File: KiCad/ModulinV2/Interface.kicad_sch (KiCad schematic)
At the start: 37 parts, among them IC2 ADS7866IDBVT, IC3 ADS7866IDBVT, IC4 ADS7041IDCUR, IC5 ADS7041IDCUR, IC6 DAC60501ZDGSR, IC7 DAC60501ZDGSR

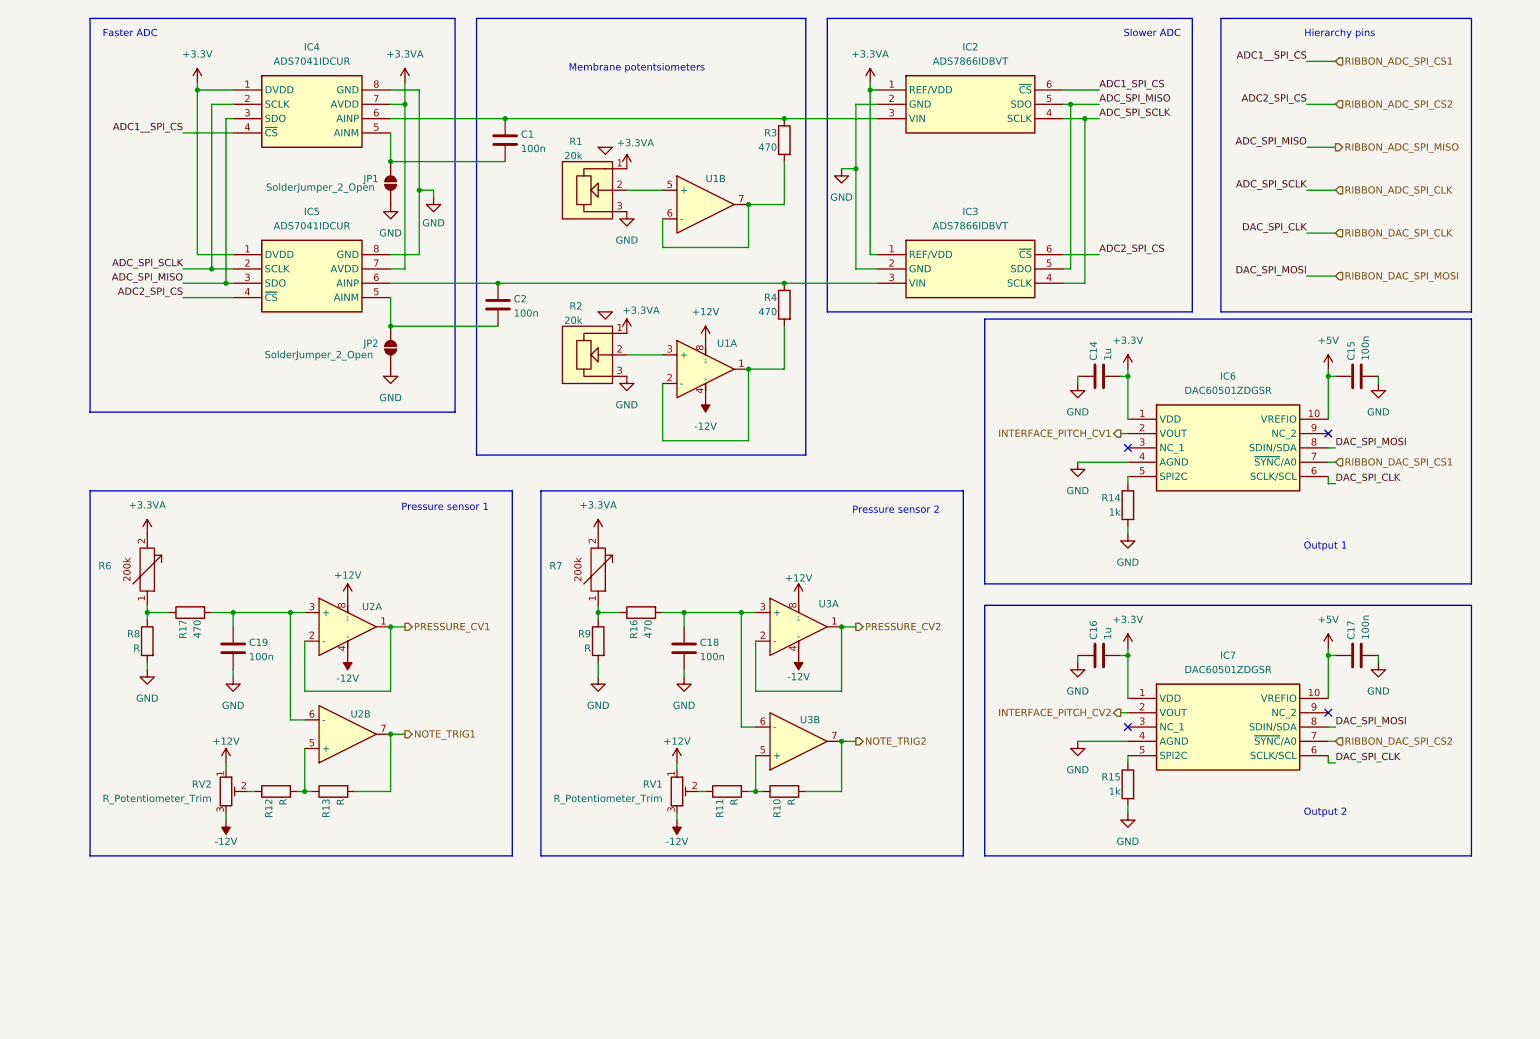
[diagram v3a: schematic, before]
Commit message: Added initial schematic of VCO and repaired some schematic issues
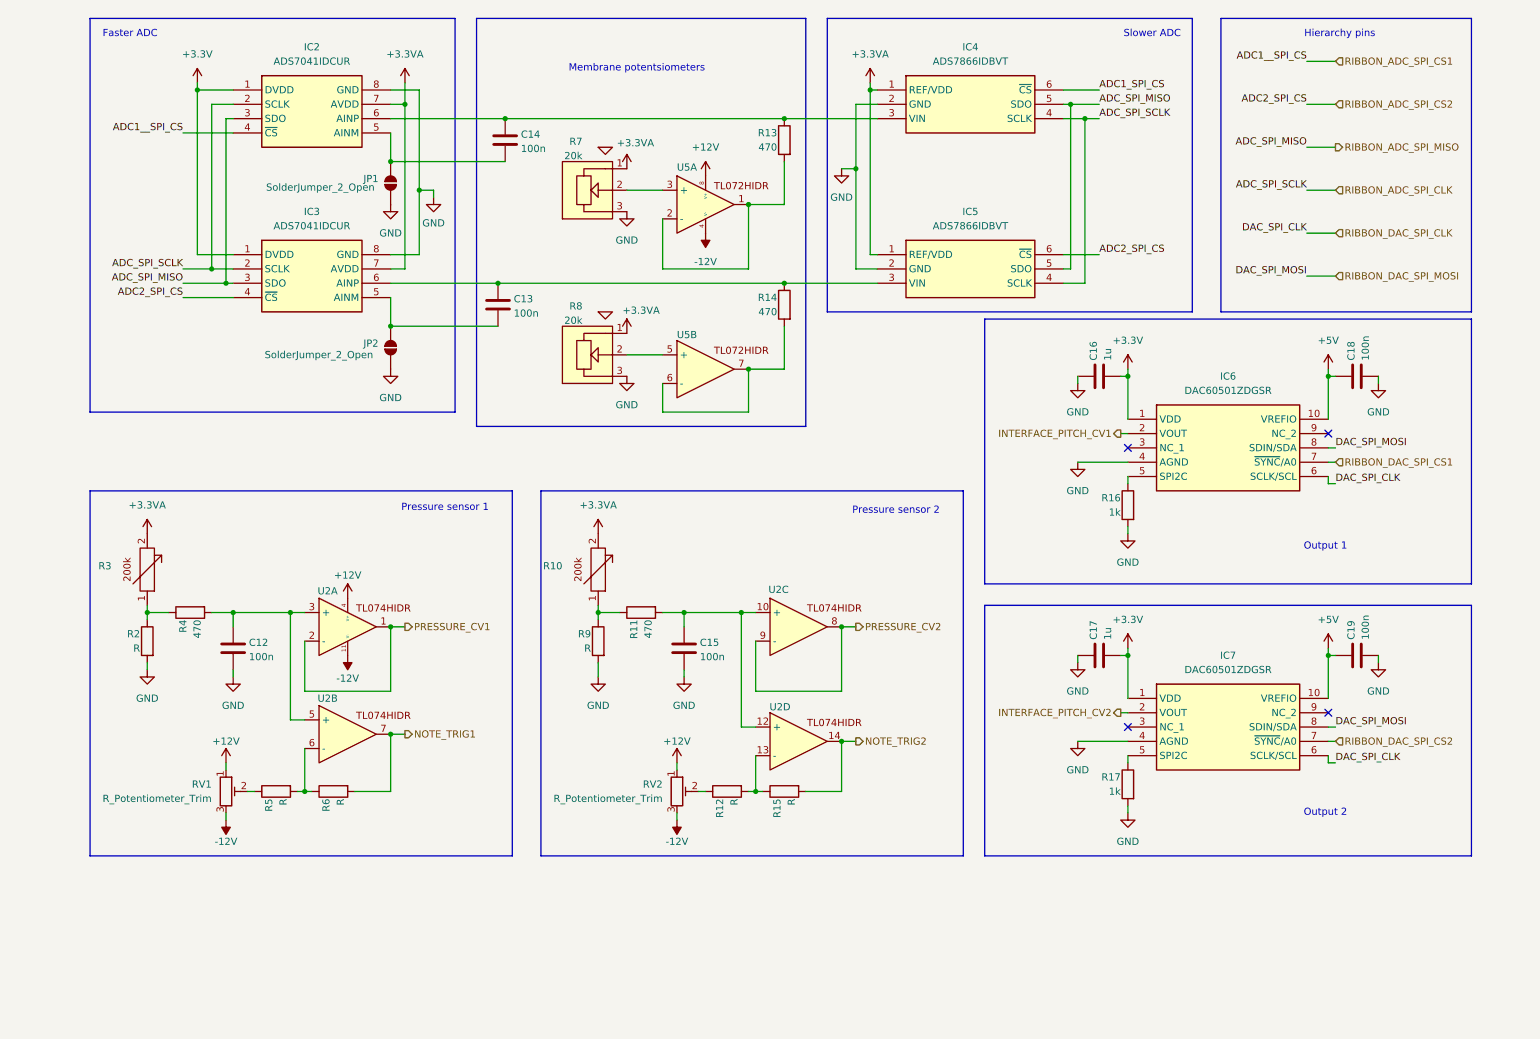
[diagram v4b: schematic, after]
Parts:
- removed U1, U2, U3: ~, symbol TL072HIDDFR:TL072HIDDFR_2
- added U2: ~, symbol TL074HIDR:TL074HIDRx4
- added U5: ~, symbol TL072HIDR:TL072HIDRx2
- renumbered C19 to C12, C2 to C13, C1 to C14, C18 to C15, C14 to C16, C16 to C17, C15 to C18, C17 to C19, IC4 to IC2, IC5 to IC3, IC2 to IC4, IC3 to IC5, R7 to R10, R16 to R11, R11 to R12, R3 to R13, R4 to R14, R10 to R15, R14 to R16, R15 to R17, R8 to R2, R6 to R3, R17 to R4, R12 to R5, R13 to R6, R1 to R7, R2 to R8, RV2 to RV1, RV1 to RV2
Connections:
- net +12V: now also U2.4 (V+), U5.8 (V+)
- net -12V: now also U2.11 (V-), U5.4 (V-)
- net NOTE_TRIG1: now also U2.7
- net NOTE_TRIG2: now also U2.14
- net PRESSURE_CV1: now also U2.1, U2.2 (-)
- net PRESSURE_CV2: now also U2.8, U2.9 (-)
- net at R13.2: now also U5.1, U5.2 (-)
- net at C15.1, R11.2: now also U2.10 (+), U2.12 (+)
- net at R14.2: now also U5.6 (-), U5.7
- net at R12.2, R15.1: now also U2.13 (-)
- net at R8.2: now also U5.5 (+)
- net at R7.2: now also U5.3 (+)
- net at C12.1, R4.2: now also U2.3 (+), U2.5 (+)
- net at R5.2, R6.1: now also U2.6 (-)

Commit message: Finished 1.0 of the VCO and started making the waveform select module
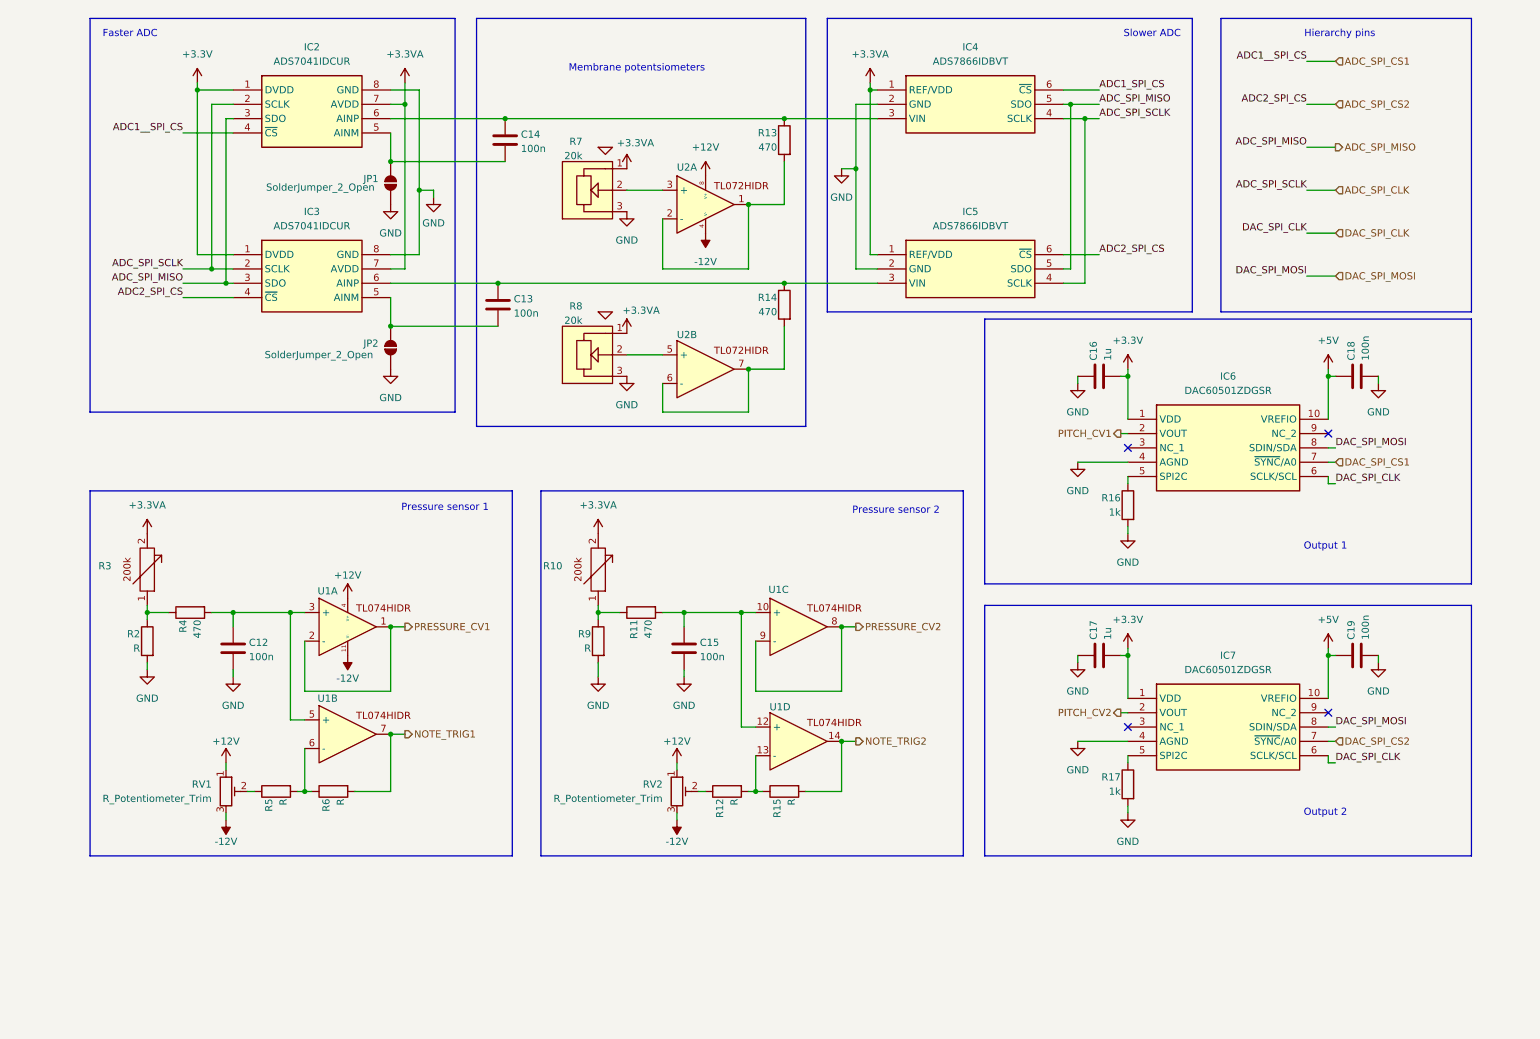
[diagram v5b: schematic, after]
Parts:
- renumbered U2 to U1, U5 to U2
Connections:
- net INTERFACE_PITCH_CV1 renamed PITCH_CV1
- net INTERFACE_PITCH_CV2 renamed PITCH_CV2
- net RIBBON_ADC_SPI_CLK renamed ADC_SPI_CLK
- net RIBBON_ADC_SPI_CS1 renamed ADC_SPI_CS1
- net RIBBON_ADC_SPI_CS2 renamed ADC_SPI_CS2
- net RIBBON_ADC_SPI_MISO renamed ADC_SPI_MISO
- net RIBBON_DAC_SPI_CLK renamed DAC_SPI_CLK
- net RIBBON_DAC_SPI_CS1 renamed DAC_SPI_CS1
- net RIBBON_DAC_SPI_CS2 renamed DAC_SPI_CS2
- net RIBBON_DAC_SPI_MOSI renamed DAC_SPI_MOSI
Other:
- company: Rasmus Palk -> (none)
- title: (none) -> Ribbon Controller interface
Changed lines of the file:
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@@
 	(paper "A4")
 	(title_block
-		(company "Rasmus Palk")
+		(title "Ribbon Controller interface")
+		(date "2025-07-13")
+		(rev "1.0")
+		(comment 1 "Instructor: Kaiser Pärnamets")
+		(comment 2 "By: Rasmus Palk")
 	)
 	(rectangle
@@
 		)
 	)
-	(hierarchical_label "RIBBON_ADC_SPI_CS1"
+	(hierarchical_label "ADC_SPI_CS1"
 		(shape input)
 		(at 247.65 22.86 0)
@@
 		)
 	)
-	(hierarchical_label "RIBBON_ADC_SPI_CLK"
+	(hierarchical_label "ADC_SPI_CLK"
 		(shape input)
 		(at 247.65 45.72 0)
@@
 		)
 	)
-	(hierarchical_label "RIBBON_DAC_SPI_CLK"
+	(hierarchical_label "DAC_SPI_CLK"
 		(shape input)
 		(at 247.65 53.34 0)
@@
 		)
 	)
-	(hierarchical_label "RIBBON_ADC_SPI_CS2"
+	(hierarchical_label "ADC_SPI_CS2"
 		(shape input)
 		(at 247.65 30.48 0)
@@
 		)
 	)
-	(hierarchical_label "RIBBON_ADC_SPI_MISO"
+	(hierarchical_label "ADC_SPI_MISO"
 		(shape output)
 		(at 247.65 38.1 0)
@@
 		)
 	)
-	(hierarchical_label "INTERFACE_PITCH_CV2"
+	(hierarchical_label "PITCH_CV2"
 		(shape output)
 		(at 209.55 138.43 180)
@@
 		)
 	)
-	(hierarchical_label "RIBBON_DAC_SPI_CS2"
+	(hierarchical_label "DAC_SPI_CS2"
 		(shape input)
 		(at 247.65 143.51 0)
@@
 		)
 	)
-	(hierarchical_label "RIBBON_DAC_SPI_MOSI"
+	(hierarchical_label "DAC_SPI_MOSI"
 		(shape input)
 		(at 247.65 60.96 0)
@@
 		)
 	)
-	(hierarchical_label "INTERFACE_PITCH_CV1"
+	(hierarchical_label "PITCH_CV1"
 		(shape output)
 		(at 209.55 88.9 180)
@@
 		)
 	)
-	(hierarchical_label "RIBBON_DAC_SPI_CS1"
+	(hierarchical_label "DAC_SPI_CS1"
 		(shape input)
 		(at 247.65 93.98 0)
@@
 		(dnp no)
 		(fields_autoplaced yes)
-		(property "Reference" "#PWR045"
+		(property "Reference" "#PWR043"
 			(at 246.38 81.28 0)
 			(effects
@@
 			(project ""
 				(path "/c6b34a57-3941-4b56-8b80-1848c7f41082/135b304f-86ea-4ef3-a69b-e7b40129e875"
-					(reference "#PWR045")
+					(reference "#PWR043")
 					(unit 1)
 				)
@@
 		(dnp no)
 		(fields_autoplaced yes)
-		(property "Reference" "#PWR047"
+		(property "Reference" "#PWR045"
 			(at 255.27 86.36 0)
 			(effects
@@
 			(project "ModulinV2"
 				(path "/c6b34a57-3941-4b56-8b80-1848c7f41082/135b304f-86ea-4ef3-a69b-e7b40129e875"
-					(reference "#PWR047")
+					(reference "#PWR045")
 					(unit 1)
 				)
@@
 		(dnp no)
 		(fields_autoplaced yes)
-		(property "Reference" "#PWR038"
+		(property "Reference" "#PWR036"
 			(at 201.93 100.33 0)
 			(effects
@@
 			(project "ModulinV2"
 				(path "/c6b34a57-3941-4b56-8b80-1848c7f41082/135b304f-86ea-4ef3-a69b-e7b40129e875"
-					(reference "#PWR038")
+					(reference "#PWR036")
 					(unit 1)
 				)
@@
 		(on_board yes)
 		(dnp no)
-		(property "Reference" "U2"
+		(property "Reference" "U1"
 			(at 149.098 137.414 0)
 			(effects
@@
 			(project ""
 				(path "/c6b34a57-3941-4b56-8b80-1848c7f41082/135b304f-86ea-4ef3-a69b-e7b40129e875"
-					(reference "U2")
+					(reference "U1")
 					(unit 4)
 				)
@@
 		(dnp no)
 		(fields_autoplaced yes)
-		(property "Reference" "#PWR035"
+		(property "Reference" "#PWR033"
 			(at 160.02 48.26 0)
 			(effects
@@
 			(project ""
 				(path "/c6b34a57-3941-4b56-8b80-1848c7f41082/135b304f-86ea-4ef3-a69b-e7b40129e875"
-					(reference "#PWR035")
+					(reference "#PWR033")
 					(unit 1)
 				)
@@
 		(on_board yes)
 		(dnp no)
-		(property "Reference" "U2"
+		(property "Reference" "U1"
 			(at 148.844 116.586 0)
 			(effects
@@
 			(project ""
 				(path "/c6b34a57-3941-4b56-8b80-1848c7f41082/135b304f-86ea-4ef3-a69b-e7b40129e875"
-					(reference "U2")
+					(reference "U1")
 					(unit 3)
 				)
@@
 		(dnp no)
 		(fields_autoplaced yes)
-		(property "Reference" "#PWR037"
+		(property "Reference" "#PWR035"
 			(at 201.93 86.36 0)
 			(effects
@@
 			(project "ModulinV2"
 				(path "/c6b34a57-3941-4b56-8b80-1848c7f41082/135b304f-86ea-4ef3-a69b-e7b40129e875"
-					(reference "#PWR037")
+					(reference "#PWR035")
 					(unit 1)
 				)
@@
 		(on_board yes)
 		(dnp no)
-		(property "Reference" "U2"
+		(property "Reference" "U1"
 			(at 68.834 116.84 0)
 			(effects
@@
 			(project ""
 				(path "/c6b34a57-3941-4b56-8b80-1848c7f41082/135b304f-86ea-4ef3-a69b-e7b40129e875"
-					(reference "U2")
+					(reference "U1")
 					(unit 1)
 				)
@@
 		(dnp no)
 		(fields_autoplaced yes)
-		(property "Reference" "#PWR044"
+		(property "Reference" "#PWR042"
 			(at 210.82 162.56 0)
 			(effects
@@
 			(project "ModulinV2"
 				(path "/c6b34a57-3941-4b56-8b80-1848c7f41082/135b304f-86ea-4ef3-a69b-e7b40129e875"
-					(reference "#PWR044")
+					(reference "#PWR042")
 					(unit 1)
 				)
@@
 		(dnp no)
 		(fields_autoplaced yes)
-		(property "Reference" "#PWR046"
+		(property "Reference" "#PWR044"
 			(at 246.38 130.81 0)
 			(effects
@@
 			(project "ModulinV2"
 				(path "/c6b34a57-3941-4b56-8b80-1848c7f41082/135b304f-86ea-4ef3-a69b-e7b40129e875"
-					(reference "#PWR046")
+					(reference "#PWR044")
 					(unit 1)
 				)
@@
 		(dnp no)
 		(fields_autoplaced yes)
-		(property "Reference" "#PWR040"
+		(property "Reference" "#PWR038"
 			(at 201.93 149.86 0)
 			(effects
@@
 			(project "ModulinV2"
 				(path "/c6b34a57-3941-4b56-8b80-1848c7f41082/135b304f-86ea-4ef3-a69b-e7b40129e875"
-					(reference "#PWR040")
+					(reference "#PWR038")
 					(unit 1)
 				)
@@
 		(dnp no)
 		(fields_autoplaced yes)
-		(property "Reference" "#PWR036"
+		(property "Reference" "#PWR034"
 			(at 165.1 30.48 0)
 			(effects
@@
 			(project "ModulinV2"
 				(path "/c6b34a57-3941-4b56-8b80-1848c7f41082/135b304f-86ea-4ef3-a69b-e7b40129e875"
-					(reference "#PWR036")
+					(reference "#PWR034")
 					(unit 1)
 				)
@@
 		(on_board yes)
 		(dnp no)
-		(property "Reference" "U2"
+		(property "Reference" "U1"
 			(at 68.834 135.89 0)
 			(effects
@@
 			(project ""
 				(path "/c6b34a57-3941-4b56-8b80-1848c7f41082/135b304f-86ea-4ef3-a69b-e7b40129e875"
-					(reference "U2")
+					(reference "U1")
 					(unit 2)
 				)
@@
 		(on_board yes)
 		(dnp no)
-		(property "Reference" "U5"
+		(property "Reference" "U2"
 			(at 132.588 71.374 0)
 			(effects
@@
 			(project ""
 				(path "/c6b34a57-3941-4b56-8b80-1848c7f41082/135b304f-86ea-4ef3-a69b-e7b40129e875"
-					(reference "U5")
+					(reference "U2")
 					(unit 2)
 				)
@@
 		(dnp no)
 		(fields_autoplaced yes)
-		(property "Reference" "#PWR041"
+		(property "Reference" "#PWR039"
 			(at 210.82 81.28 0)
 			(effects
@@
 			(project ""
 				(path "/c6b34a57-3941-4b56-8b80-1848c7f41082/135b304f-86ea-4ef3-a69b-e7b40129e875"
-					(reference "#PWR041")
+					(reference "#PWR039")
 					(unit 1)
 				)
@@
 		(dnp no)
 		(fields_autoplaced yes)
-		(property "Reference" "#PWR048"
+		(property "Reference" "#PWR046"
 			(at 255.27 135.89 0)
 			(effects
@@
 			(project "ModulinV2"
 				(path "/c6b34a57-3941-4b56-8b80-1848c7f41082/135b304f-86ea-4ef3-a69b-e7b40129e875"
-					(reference "#PWR048")
+					(reference "#PWR046")
 					(unit 1)
 				)
@@
 		(dnp no)
 		(fields_autoplaced yes)
-		(property "Reference" "#PWR043"
+		(property "Reference" "#PWR041"
 			(at 210.82 130.81 0)
 			(effects
@@
 			(project "ModulinV2"
 				(path "/c6b34a57-3941-4b56-8b80-1848c7f41082/135b304f-86ea-4ef3-a69b-e7b40129e875"
-					(reference "#PWR043")
+					(reference "#PWR041")
 					(unit 1)
 				)
@@
 		(dnp no)
 		(fields_autoplaced yes)
-		(property "Reference" "#PWR039"
+		(property "Reference" "#PWR037"
 			(at 201.93 135.89 0)
 			(effects
@@
 			(project "ModulinV2"
 				(path "/c6b34a57-3941-4b56-8b80-1848c7f41082/135b304f-86ea-4ef3-a69b-e7b40129e875"
-					(reference "#PWR039")
+					(reference "#PWR037")
 					(unit 1)
 				)
@@
 		(dnp no)
 		(fields_autoplaced yes)
-		(property "Reference" "#PWR042"
+		(property "Reference" "#PWR040"
 			(at 210.82 113.03 0)
 			(effects
@@
 			(project ""
 				(path "/c6b34a57-3941-4b56-8b80-1848c7f41082/135b304f-86ea-4ef3-a69b-e7b40129e875"
-					(reference "#PWR042")
+					(reference "#PWR040")
 					(unit 1)
 				)
@@
 		(on_board yes)
 		(dnp no)
-		(property "Reference" "U5"
+		(property "Reference" "U2"
 			(at 132.588 41.656 0)
 			(effects
@@
 			(project ""
 				(path "/c6b34a57-3941-4b56-8b80-1848c7f41082/135b304f-86ea-4ef3-a69b-e7b40129e875"
-					(reference "U5")
+					(reference "U2")
 					(unit 1)
 				)
